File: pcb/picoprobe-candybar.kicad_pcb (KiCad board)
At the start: 2 copper layers, 27.9 x 97.9 mm, 39 parts, among them J0 SWD-UART_PicoprobeCandybar, J1 PinHeader_2x04, J2 PinSocket_1x03, J3 PinSocket_1x03, J4 PinSocket_1x03, J5 PinSocket_1x03, J6 PinSocket_1x03, J7 PinSocket_1x03, Q1 T2N7002AK, Q2 DMP31D1U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

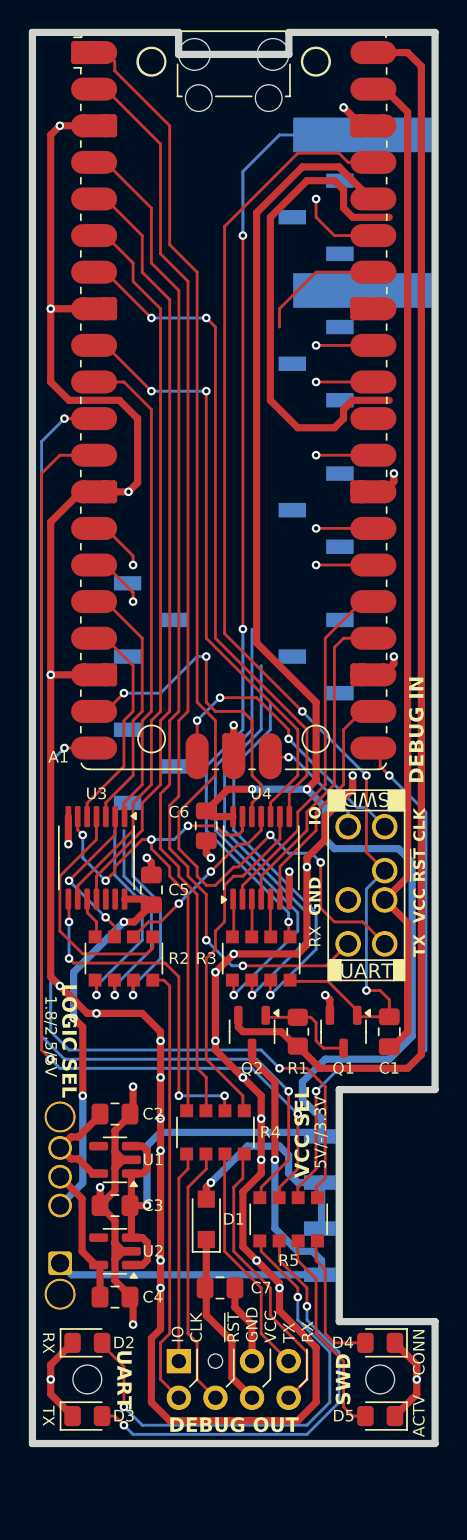
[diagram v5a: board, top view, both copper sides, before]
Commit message: Continue refining layout; add SMD PinHeader
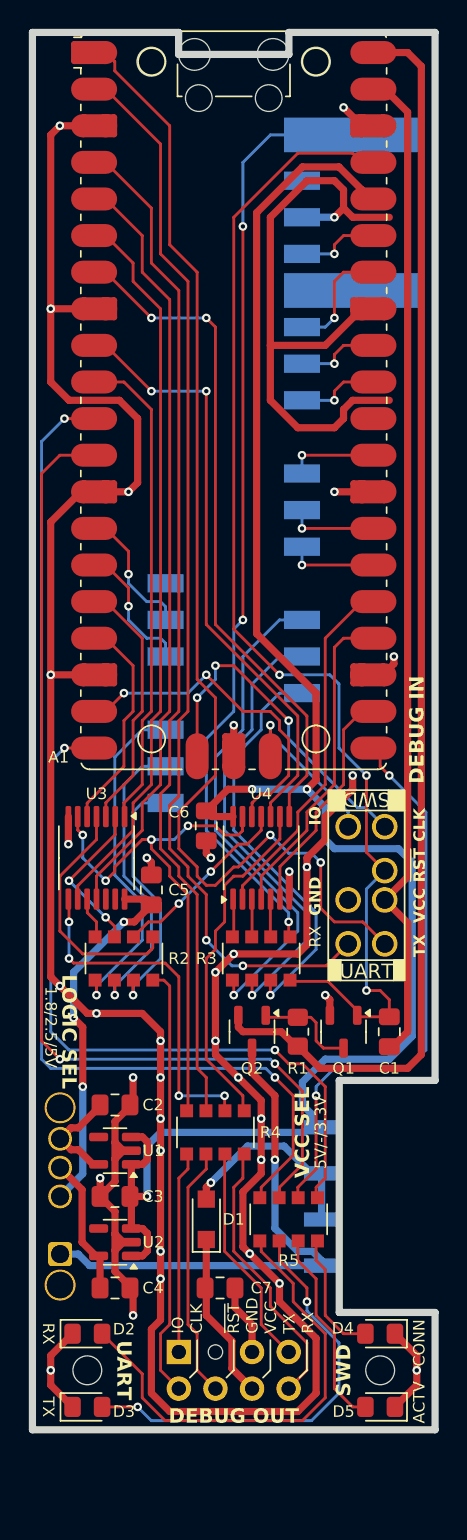
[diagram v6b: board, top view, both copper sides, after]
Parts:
- J2, J3, J4, J5, J6, J7: footprint Connector_PinSocket_2.54mm:PinSocket_1x03_P2.54mm_Vertical_SMD_Pin1Left -> ProjectFootprints_PicoprobeCandybar:PinHeader_1x03_P2.54mm_Horizontal_SMD
- moved J2 2.54 mm to (93.3, 111.1), turned to 180 degrees
- moved J3 2.54 mm to (93.3, 101.0), turned to 180 degrees
- moved J4 2.54 mm to (109.9, 103.5), turned to 0 degrees
- moved J5 2.54 mm to (109.9, 93.3), turned to 0 degrees
- moved J6 2.54 mm to (109.9, 83.2), turned to 0 degrees
- moved J7 2.54 mm to (109.9, 73.0), turned to 0 degrees
- moved D3 0.64 mm to (91.4, 155.6)
- moved D5 0.64 mm to (111.8, 155.6)
- moved J1 0.64 mm to (97.8, 151.8)
- moved D2 0.63 mm to (91.4, 150.5)
- moved D4 0.63 mm to (111.8, 150.5)
- moved REF** 0.63 mm to (111.8, 153.0)
- moved REF** 0.63 mm to (91.4, 153.0)
- moved SW1 0.63 mm to (85.1, 78.1)
- moved SW2 0.63 mm to (115.6, 141.0)
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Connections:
- J2 pad 1: /CB_CTS -> /CB_DTR
- J2 pad 3: /CB_DTR -> /CB_CTS
- J3 pad 2: /INT_FALL -> /INT_RISE
- J3 pad 3: /INT_RISE -> /INT_FALL
- J4 pad 1: /CB_RS3 -> /CB_RS1
- J4 pad 3: /CB_RS1 -> /CB_RS3
- J5 pad 1: /CB_RS6 -> /CB_RS4
- J5 pad 3: /CB_RS4 -> /CB_RS6
- J6 pad 1: /ADC2 -> /ADC0
- J6 pad 3: /ADC0 -> /ADC2
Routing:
- net AGND: track 34.0 -> 44.6 mm, vias 0 -> 1
- net /CB_DTR: track 14.6 -> 24.0 mm
- net /CB_RTS: track 14.3 -> 20.9 mm
- net /INT_FALL: track 3.33 -> 8.63 mm
- net /INT_RISE: track 3.33 -> 8.63 mm
- net /CB_CTS: track 14.1 -> 17.8 mm
- net Net-(A1-SWCLK): track 19.4 -> 23.1 mm
- net GND: track 239.7 -> 236.7 mm
- net /CB_RS3: track 31.7 -> 34.7 mm
- net /CB_RS2: track 28.9 -> 31.6 mm
- net /CB_RS1: track 26.1 -> 28.6 mm
- net /CB_RS6: track 3.17 -> 5.43 mm
- net /CB_RS5: track 3.17 -> 5.42 mm
- net /CB_RS4: track 3.17 -> 5.42 mm
- net Net-(A1-SWDIO): track 9.50 -> 11.5 mm
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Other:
- board size 27.9 x 97.9 mm -> 27.9 x 97 mm

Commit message: Continue refining layout; accommodate courtyards
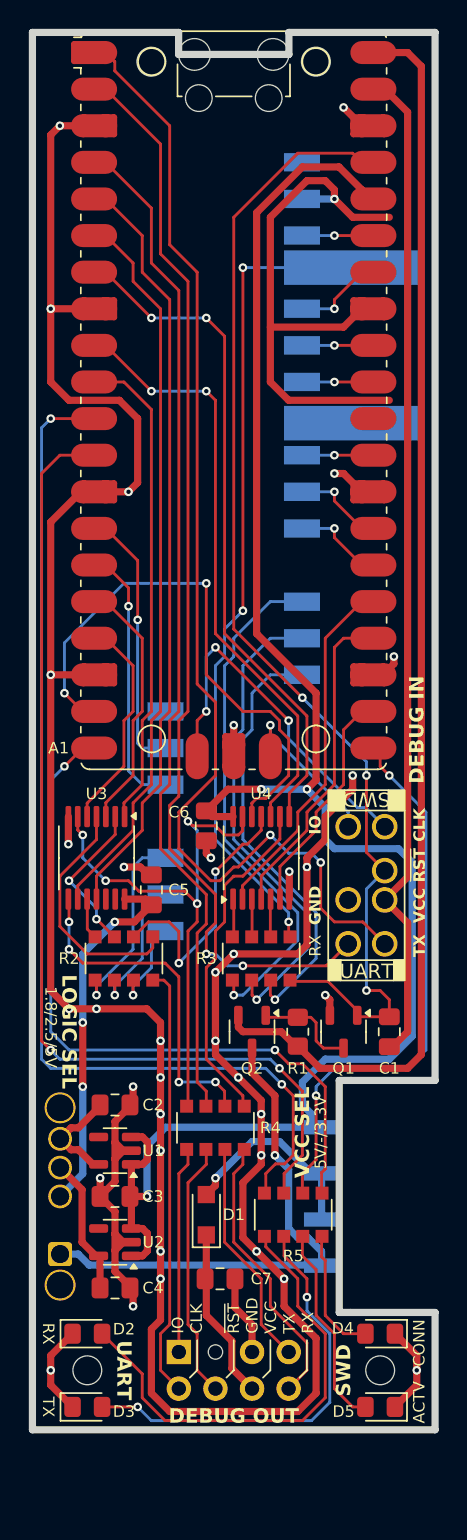
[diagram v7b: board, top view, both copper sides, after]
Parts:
- REF** (x4): moved to B.Cu
- moved SW1 9.21 mm to (85.1, 87.3)
- moved J2 8.89 mm to (93.3, 120.0)
- moved J3 8.89 mm to (93.3, 109.9)
- moved J7 1.27 mm to (109.9, 71.8)
- moved J4 1.27 mm to (109.9, 102.2)
- moved J5 1.27 mm to (109.9, 92.1)
- moved J6 1.27 mm to (109.9, 81.9)
- moved C7 0.63 mm to (100.6, 146.7)
- moved R5 0.45 mm to (105.7, 142.2)
- moved D1 0.32 mm to (99.7, 142.2)
- moved R4 0.32 mm to (100.3, 136.2)
- turned REF** to 180 degrees (x4)
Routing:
- net /IO_IN: track 22.8 -> 39.5 mm
- net /CB_CTS: track 17.8 -> 6.74 mm
- net /CB_RTS: track 20.9 -> 9.84 mm
- net /CB_DTR: track 24.0 -> 13.5 mm
- net /INT_RISE: track 8.63 -> 17.9 mm
- net /INT_FALL: track 8.63 -> 17.9 mm
- net Net-(R3D-R4.2): track 65.0 -> 57.0 mm
- net Net-(R2C-R3.2): track 12.9 -> 18.8 mm
- net AGND: track 44.6 -> 40.1 mm
- net /3V3_EN: track 83.1 -> 81.0 mm
- net Net-(A1-SWCLK): track 23.1 -> 24.9 mm
- net /CB_RS2: track 31.6 -> 33.4 mm
- net /CB_RS1: track 28.6 -> 30.3 mm
- net /ADC2: track 7.22 -> 5.58 mm
- net GND: track 236.7 -> 238.3 mm
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
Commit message: Update candybar-interface to 'swd-only' HEAD
Reorders `RST`, `GND`, and `VCC`.
Needed in order to bring Candybar layout to parity.
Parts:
- J0: footprint Connector_PicoprobeCandybar:SWD-UART_PicoprobeCandybar_2Rows_7Pins_P2.54mm_Polarized_PressFit_Vertical -> Connector_PicoprobeCandybar:SWD-UART_PicoprobeCandybar_PressFit
- moved J0 4.02 mm to (110.8, 119.4)
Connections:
- J0 pad 4: /3V3_EN -> VSYS
- J0 pad 6: VSYS -> /3V3_EN
